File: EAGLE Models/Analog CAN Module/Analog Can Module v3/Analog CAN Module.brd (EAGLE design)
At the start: 103.3 x 85.1 mm, 256 parts, among them IC1 AT90CAN128, IC2 MCP2551SO8, IC3 NUP2105L, IC5 FT232RL, Q1 56P2859, U1 LTC2053, U10 LTC2053, U11 LTC2053, U12 LTC2053, U13 LTC2053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

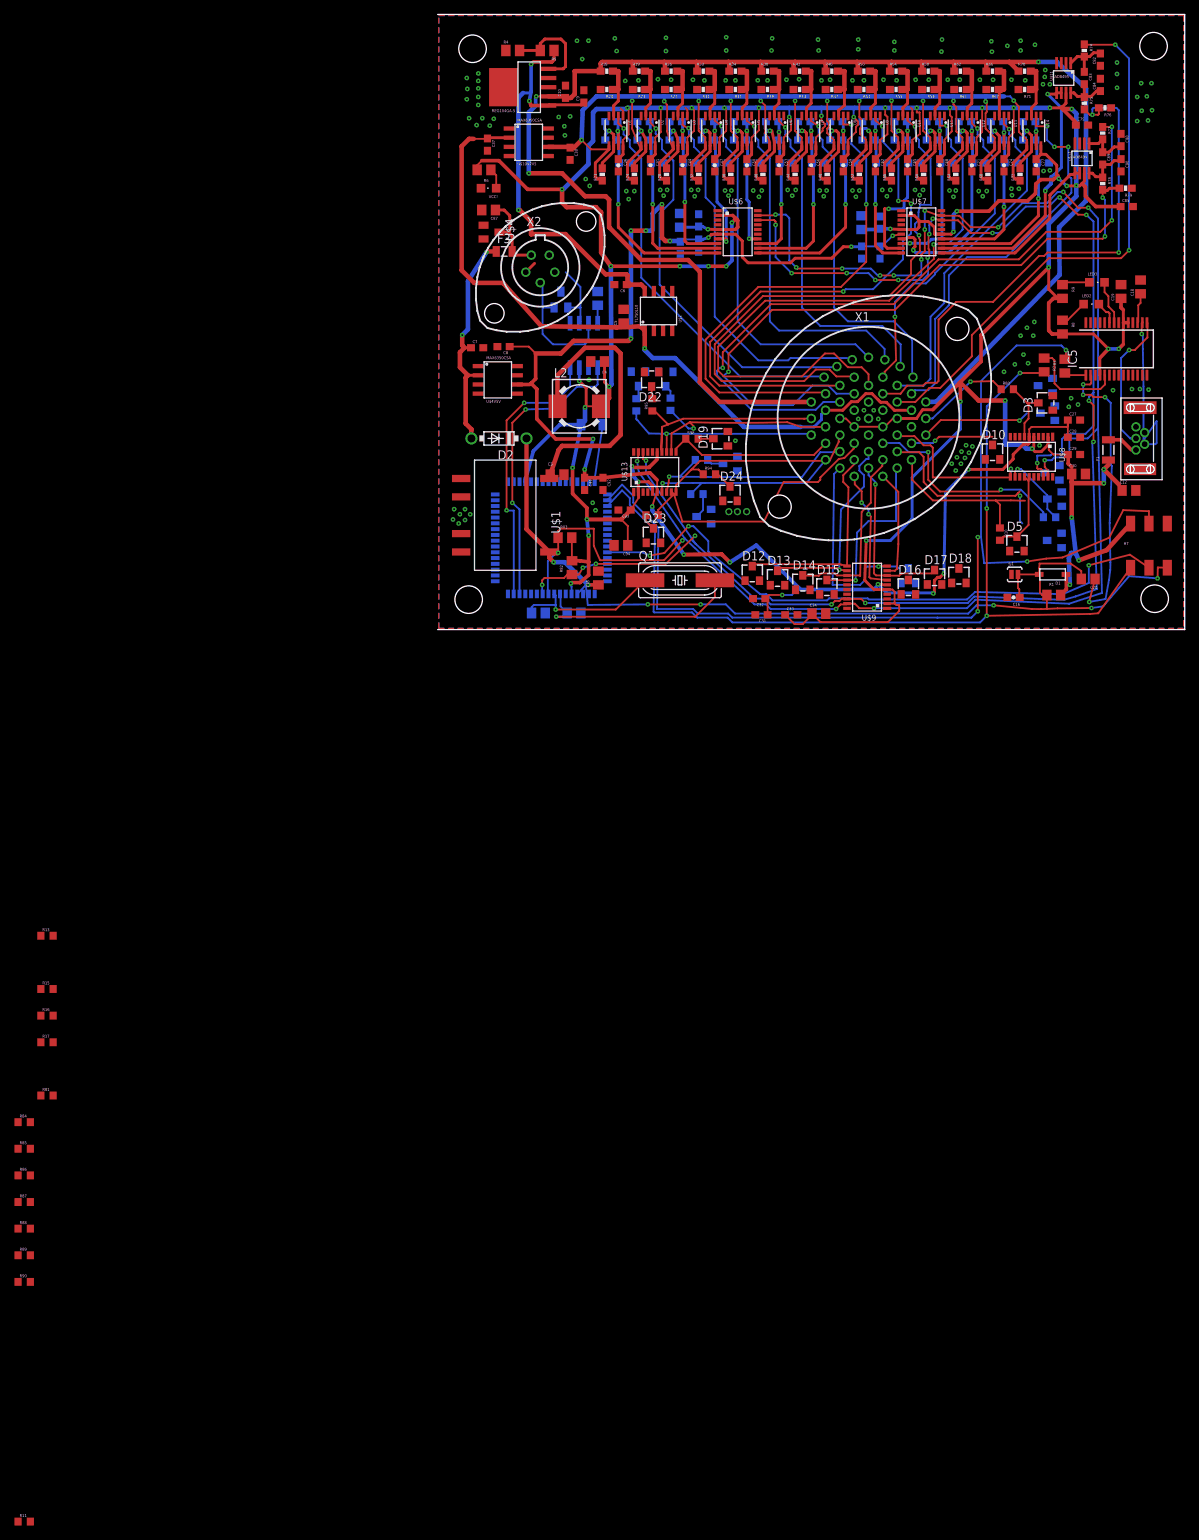
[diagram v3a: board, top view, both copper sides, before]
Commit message: Added all resistors to board
everything fits but many traces need to be rerouted to 45 degree angles
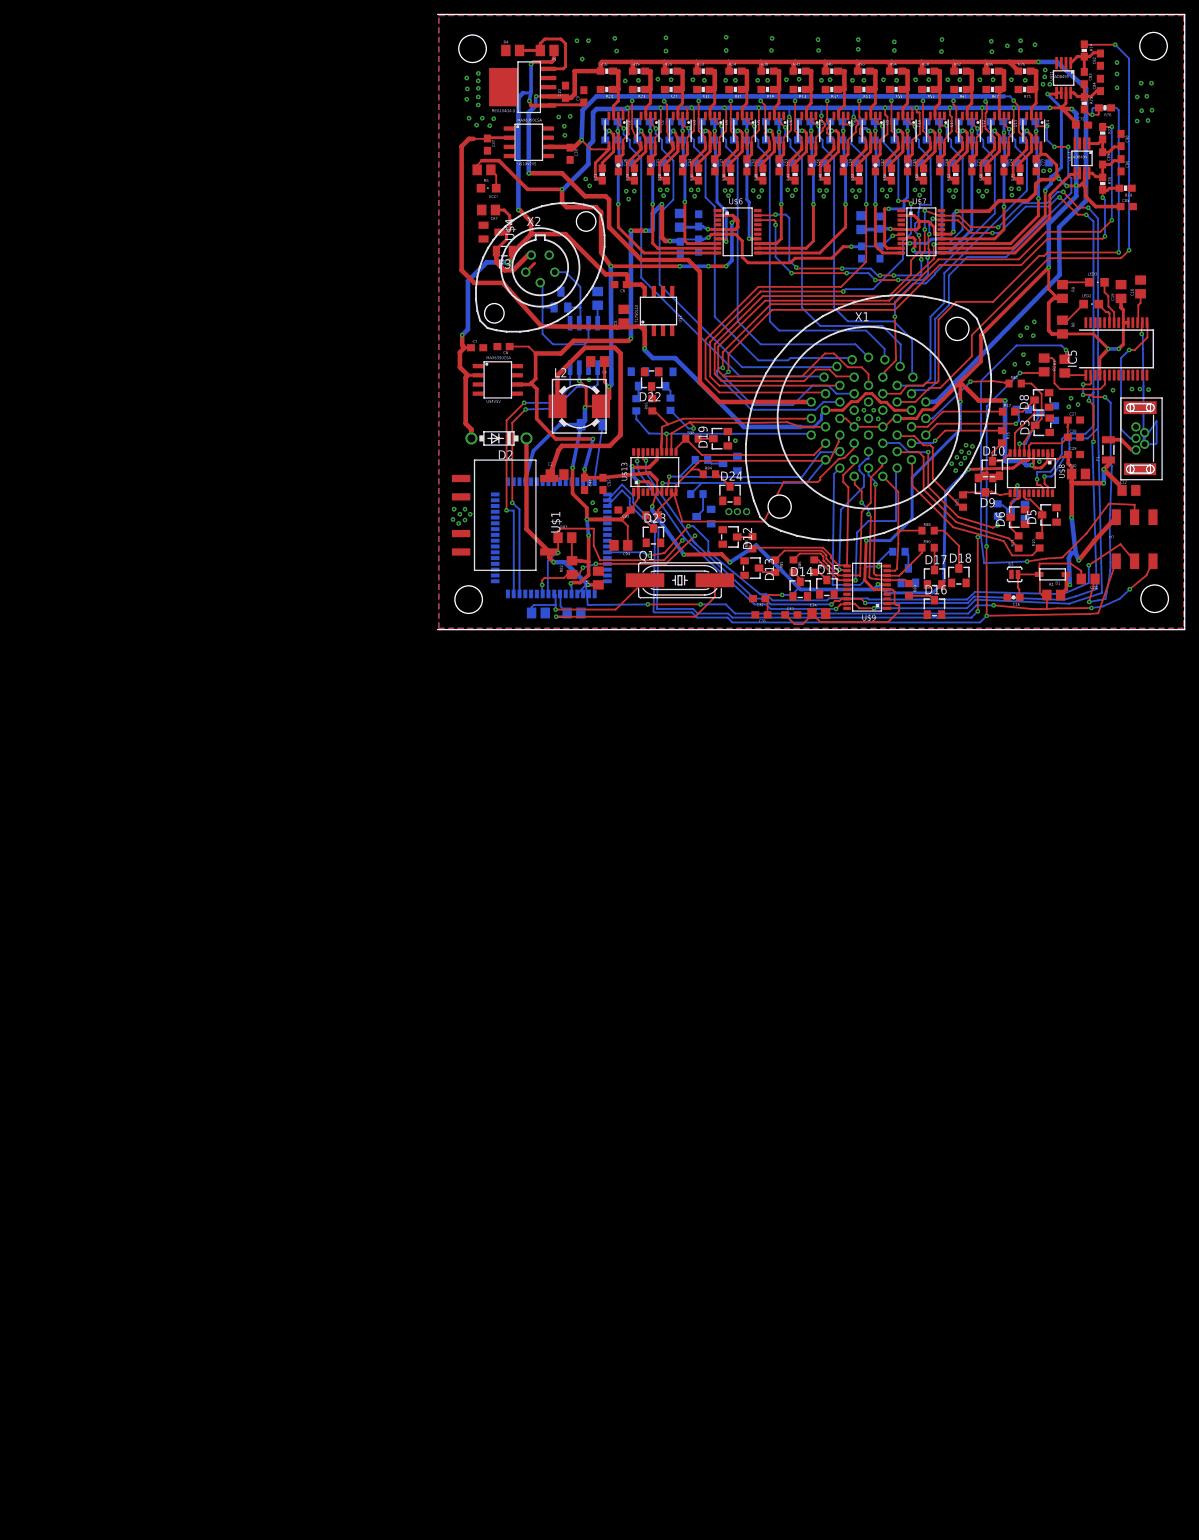
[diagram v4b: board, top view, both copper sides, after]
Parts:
- moved R11 180.6 mm to (63.8, 10.8), flipped to the bottom, turned to 180 degrees
- moved R81 164.9 mm to (80.9, 30.4), flipped to the bottom, turned to 180 degrees
- moved R90 161.1 mm to (67.8, 11.3)
- moved R17 159.0 mm to (79.0, 30.1)
- moved R88 158.0 mm to (67.8, 13.7)
- moved R16 154.5 mm to (78.1, 26.7), turned to 270 degrees
- moved R89 153.1 mm to (65.2, 5.51), turned to 270 degrees
- moved R13 145.0 mm to (80.4, 12.1), turned to 90 degrees
- moved R15 143.5 mm to (72.7, 17.8), turned to 90 degrees
- moved R87 140.3 mm to (52.1, 8.79), turned to 270 degrees
- moved R86 135.7 mm to (49.2, 8.79), turned to 270 degrees
- moved R85 131.5 mm to (46.7, 8.79), turned to 270 degrees
- moved R84 128.7 mm to (43.6, 12.0), turned to 90 degrees
- moved D9 9.38 mm to (75.8, 20.0), flipped to the top, turned to 180 degrees
- moved R14 7.23 mm to (77.5, 16.5), turned to 90 degrees
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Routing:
- net A3: track 0.00 -> 13.4 mm
- net A3CC: track 0.09 -> 11.9 mm
- net A2CC: track 0.00 -> 8.69 mm, vias 0 -> 1
- net A11CC: track 0.00 -> 7.41 mm
- net A7CC: track 0.00 -> 7.20 mm
- net A4CC: track 0.00 -> 6.04 mm
- net 12V: track 91.9 -> 97.8 mm
- net 12V_PREPTC: track 11.6 -> 16.9 mm
- net A5CC: track 1.67 -> 6.81 mm, vias 1 -> 0
- net A6: track 29.3 -> 24.6 mm
- net A5: track 20.5 -> 15.8 mm
- net A8CC: track 11.7 -> 7.37 mm
- net A9CC: track 0.00 -> 3.76 mm
- net A11: track 15.2 -> 18.6 mm
- net A9: track 17.5 -> 20.7 mm
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
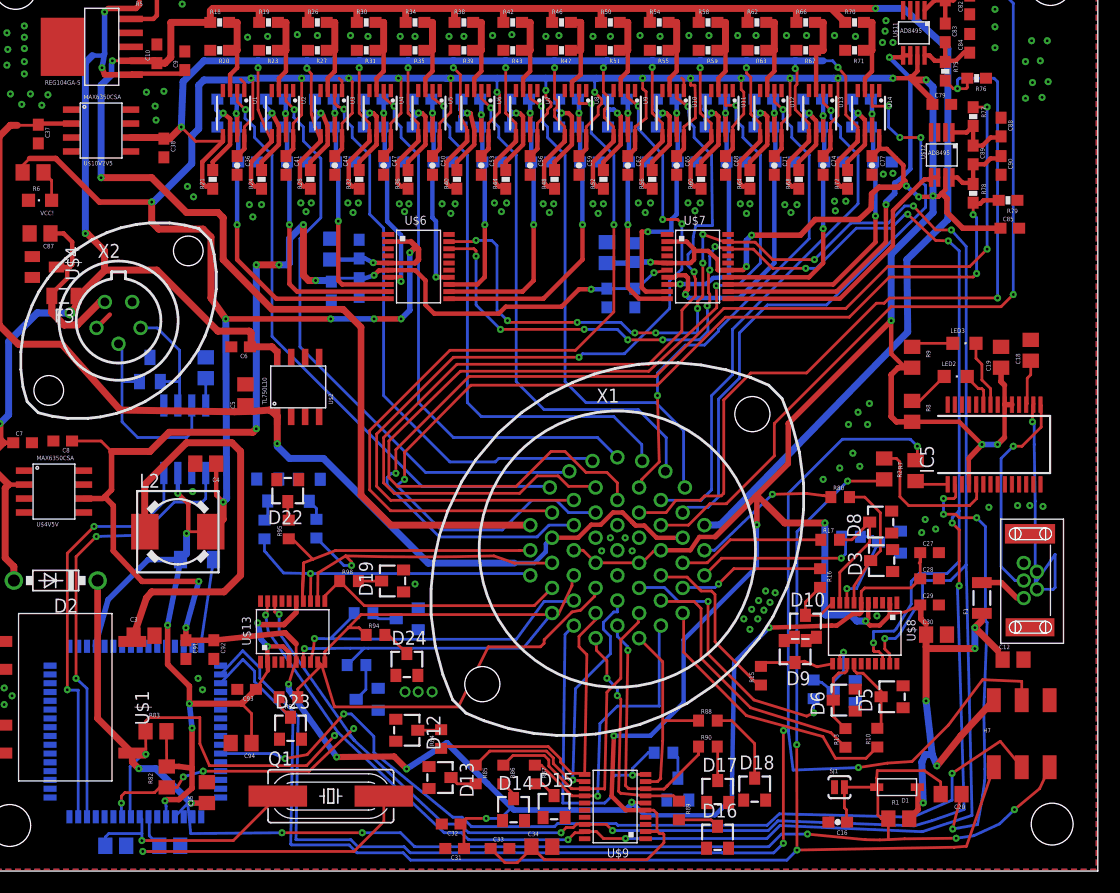
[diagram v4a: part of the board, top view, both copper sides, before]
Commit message: Rearanged traces and fixed drc errors
rearanged most of the traces to be at 45 degree angles and fixed many of
the overlapping and clearance drc errors on the board.
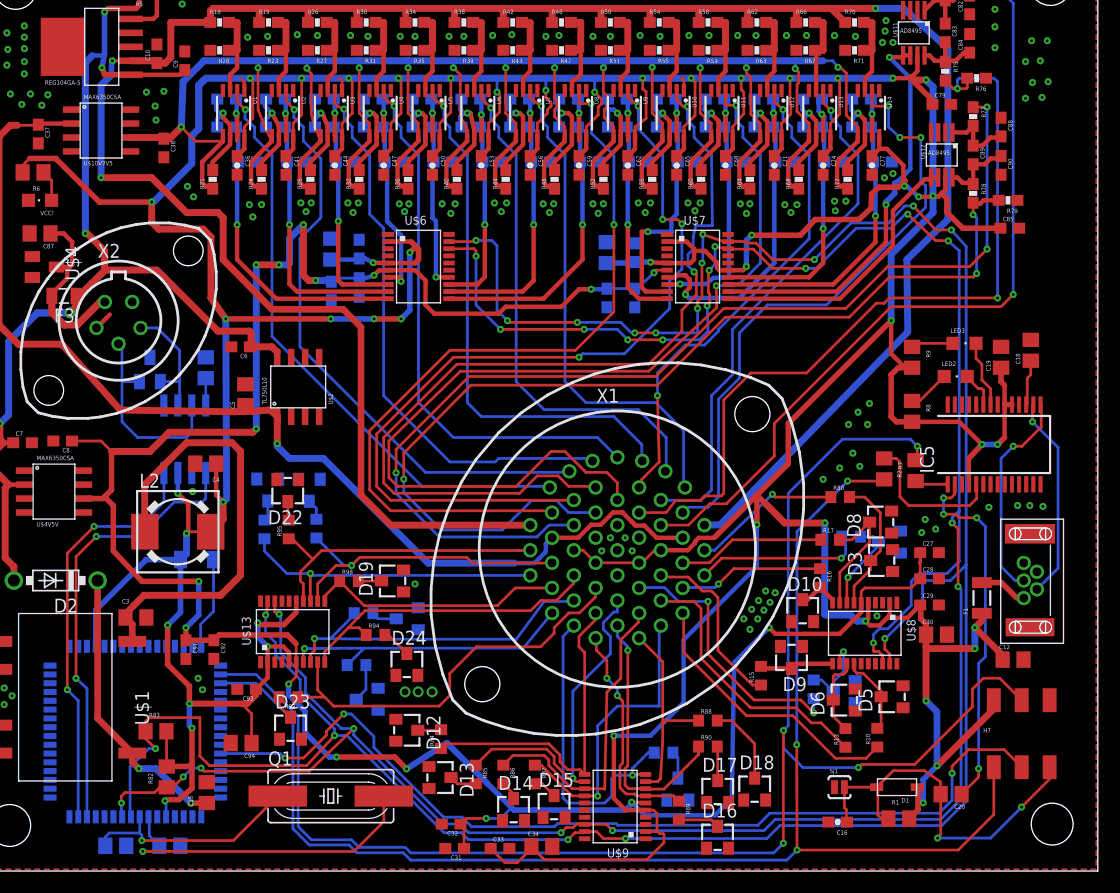
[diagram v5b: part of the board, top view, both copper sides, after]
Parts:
- moved C3 1.81 mm to (15.8, 23.1)
- moved D10 1.44 mm to (76.5, 23.7)
- moved D9 0.63 mm to (75.5, 19.4)
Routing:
- net RESET: track 106.9 -> 35.4 mm, vias 5 -> 2
- net DTR: track 40.9 -> 33.1 mm
- net D-: track 24.4 -> 18.7 mm
- net VCC: track 665.5 -> 670.6 mm
- net RX: track 144.8 -> 140.8 mm
- net TX: track 130.6 -> 127.7 mm
- net A24: track 30.4 -> 27.6 mm
- net A4CC: track 6.04 -> 3.93 mm
- net 5VREF: track 218.7 -> 220.8 mm
- net N$13: track 39.8 -> 41.3 mm
- net A22: track 29.8 -> 28.4 mm
- net SDA: track 238.3 -> 237.4 mm
- net TCI2+: track 98.7 -> 97.8 mm
- net A19: track 38.3 -> 37.4 mm
- net SGO13: track 26.3 -> 27.0 mm
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
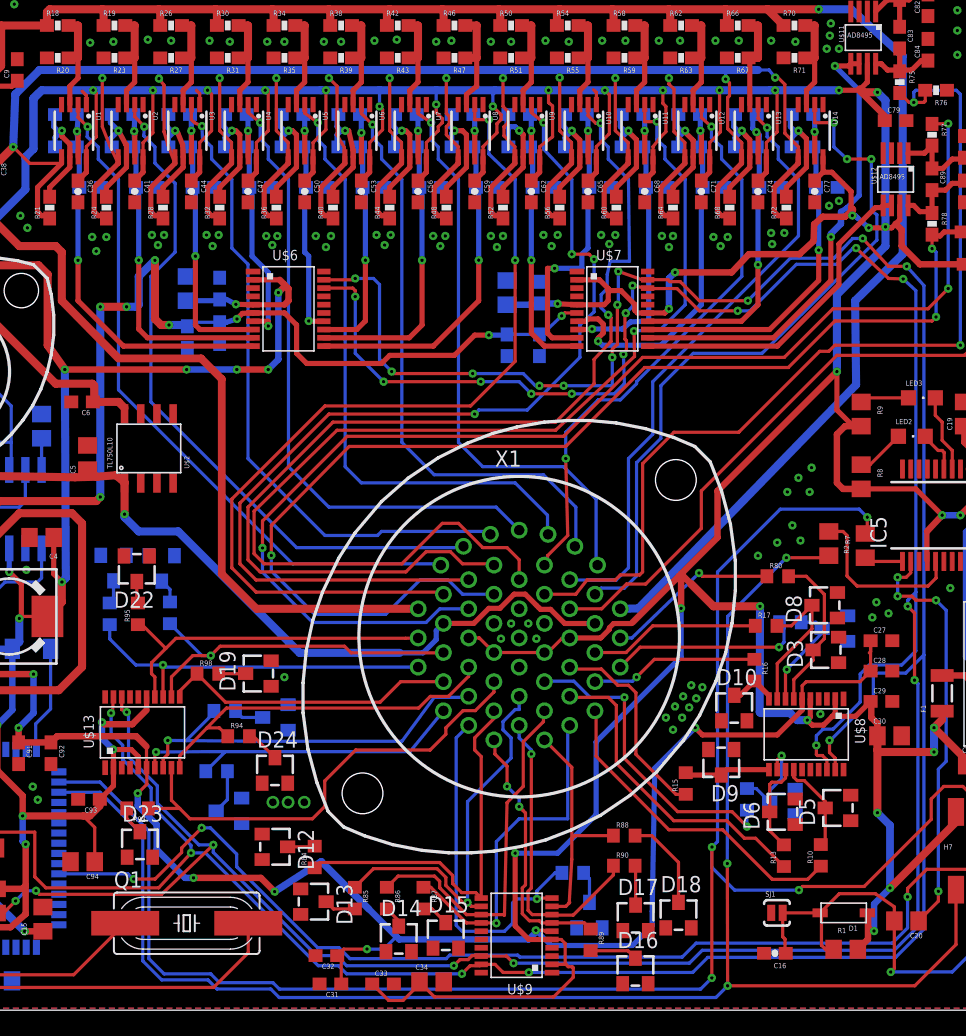
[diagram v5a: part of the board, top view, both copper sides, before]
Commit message: Finishing touches on Analog CAN and Increasing 12V trace on Daughter Card
Fixed some traces and DRC's on Analog CAN
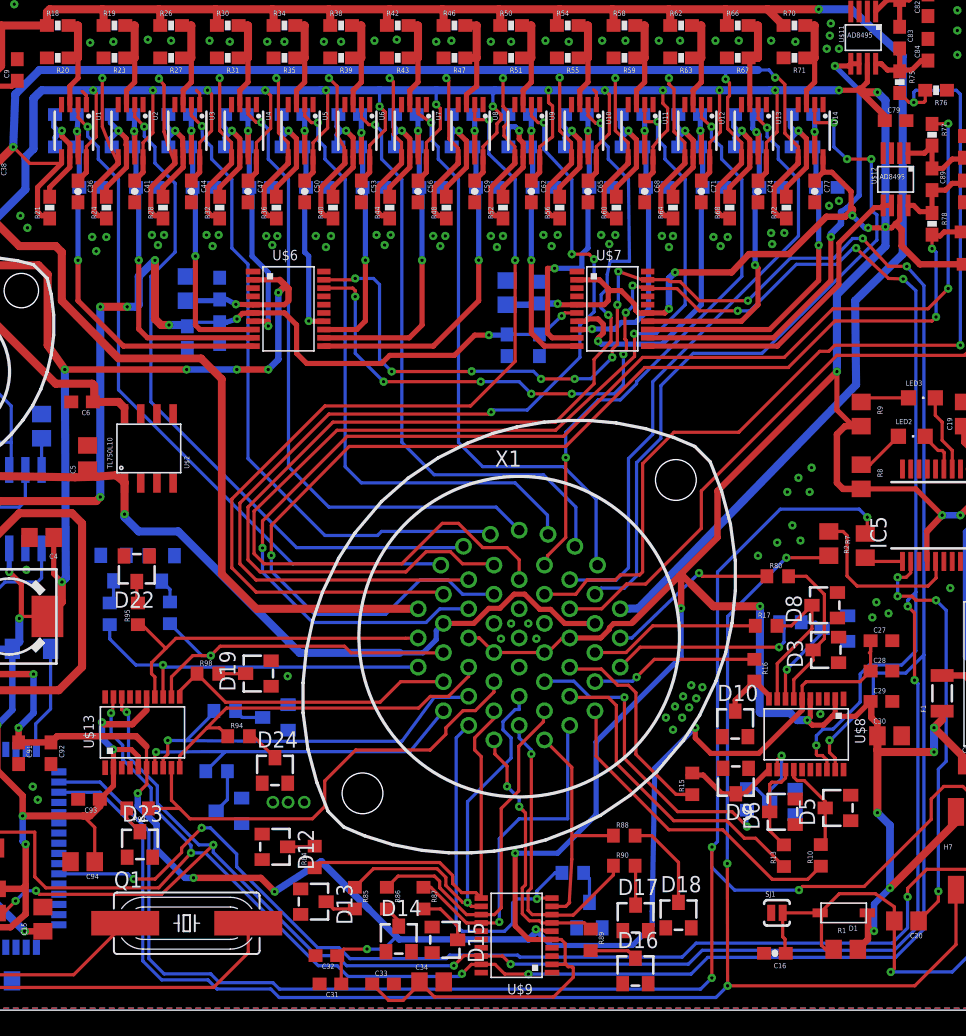
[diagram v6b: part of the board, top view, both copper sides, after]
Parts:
- moved D9 1.86 mm to (76.6, 18.0)
- moved D10 1.25 mm to (76.5, 22.5)
- moved R15 0.51 mm to (73.2, 17.8)
- moved D15 0.36 mm to (53.8, 5.52), turned to 270 degrees
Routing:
- net A16CC: track 2.19 -> 4.31 mm
- net 5VREF: track 220.8 -> 222.6 mm
- net SCL: track 242.8 -> 241.3 mm
- net A5CC: track 6.78 -> 8.09 mm
- net VCC: track 670.6 -> 669.4 mm
- net A5: track 16.3 -> 17.3 mm
- net A4CC: track 3.93 -> 4.87 mm
- net 2V5REF: track 262.2 -> 261.5 mm
